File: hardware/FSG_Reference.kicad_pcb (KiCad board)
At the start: 2 copper layers, 63.5 x 38 mm, 73 parts, among them J1 D369-B66-NP4, J3 Screw_Terminal_01x02, K1 SANYOU_SRD_Form_C, Q1 BSS138, Q2 Si2319CDS, Q3 BSS138, U1 LM393, U2 LM393, U3 LM393, U4 LM1117-5.0, U5 LM393, U6 74AHC1G02, U7 MC78M12CDTG DPAK

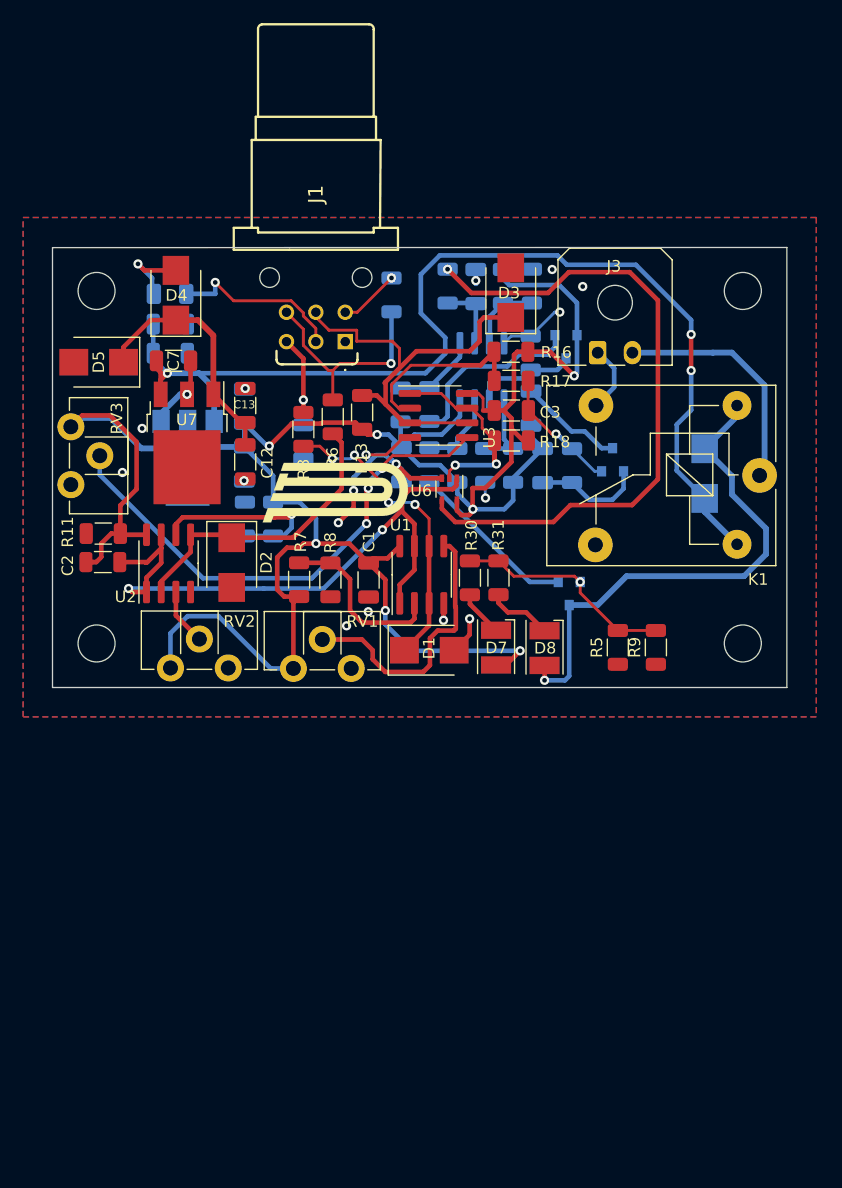
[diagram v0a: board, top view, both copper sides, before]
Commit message: Changed the connector
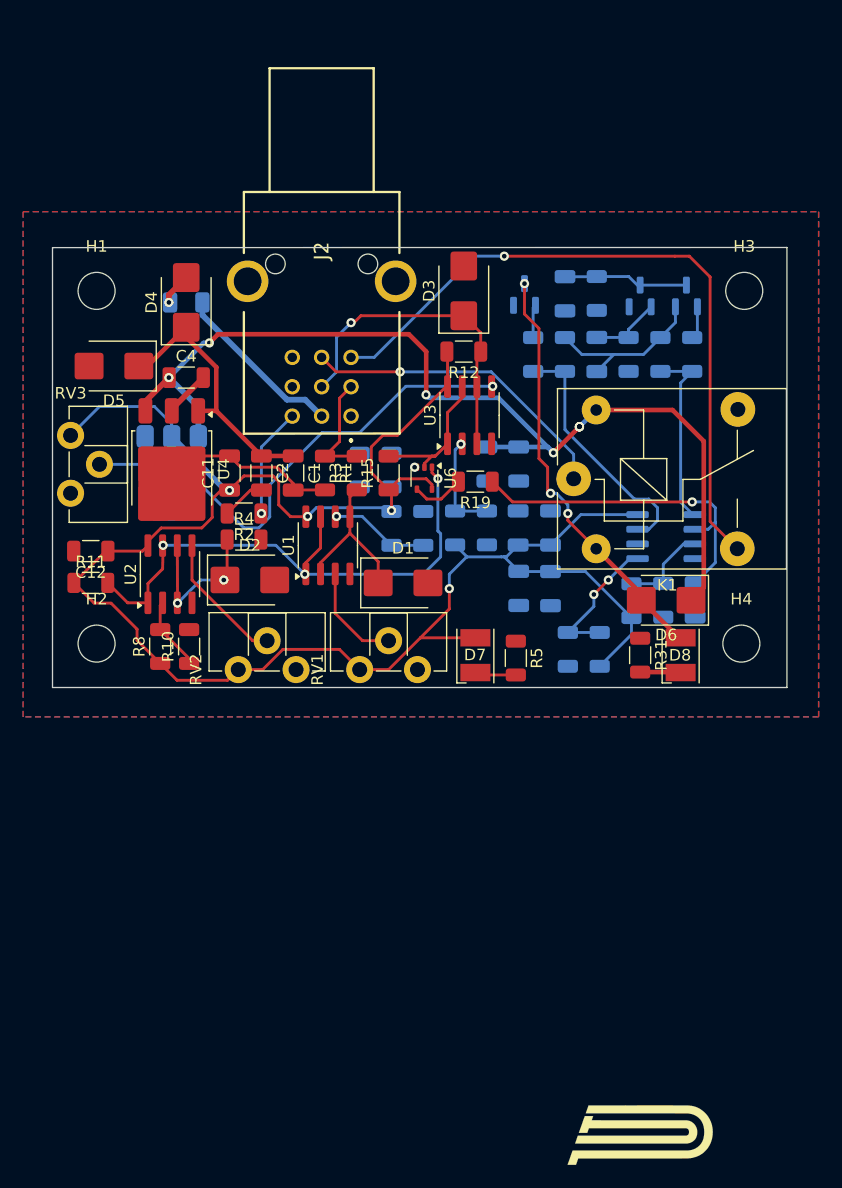
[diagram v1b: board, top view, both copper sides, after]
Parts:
- removed C15: 100n, Capacitor_SMD:C_1206_3216Metric
- removed J1: D369-B66-NP4, Library:D369B66NP4
- removed J3: Screw_Terminal_01x02, Connector_Molex:Molex_Micro-Fit_3.0_43650-0200_1x02_P3.00mm_Horizontal
- removed R17, R18: 10k, Resistor_SMD:R_1206_3216Metric
- removed R30: 1k, Resistor_SMD:R_1206_3216Metric
- added C14: 100n, Capacitor_SMD:C_1206_3216Metric, B.Cu at (140.8, 123.0)
- added J2: D369-G99-NP4, Connector_9pin:D369G99NP4, F.Cu at (123.5, 108.1)
- added R14: 10k, Resistor_SMD:R_1206_3216Metric, B.Cu at (135.2, 117.8)
- added R15: 10k, Resistor_SMD:R_1206_3216Metric, F.Cu at (126.8, 113.0)
- added R2: 100k, Resistor_SMD:R_1206_3216Metric, F.Cu at (114.2, 116.5)
- C1: value 100n -> 10u
- C11, D6, R1, R12, R19: moved to F.Cu
- C12: value 10u -> 100n
- C13: value 100n -> 10u; moved to B.Cu
- C3, C7, R9: moved to B.Cu
- C4: value 10u -> 100n; moved to F.Cu
- R10, R4: value 100k -> 10k; moved to F.Cu
- R13, R6: value 10k -> 100k; moved to B.Cu
- R16: value 100k -> 0R; moved to B.Cu
- R5: value 0R -> 1k
- R7: value 100k -> 10k; moved to B.Cu
- R8: value 10k -> 100k
- U4: value LM1117-5.0 -> MC78M12CDTG DPAK; footprint Package_TO_SOT_SMD:SOT-223 -> Package_TO_SOT_SMD:TO-252-3_TabPin2; moved to F.Cu
- U7: value MC78M12CDTG DPAK -> LM1117-5.0; footprint Package_TO_SOT_SMD:TO-252-3_TabPin2 -> Package_TO_SOT_SMD:SOT-223; moved to B.Cu
- moved G*** 61.5 mm to (148.1, 170.1)
- moved C7 33.1 mm to (137.9, 117.8), turned to 90 degrees
- moved C5 33.1 mm to (153.2, 124.0), turned to -90 degrees
- moved R22 29.4 mm to (150.5, 124.0), turned to -90 degrees
- moved R21 29.4 mm to (147.8, 124.0), turned to 90 degrees
- moved C13 28.4 mm to (138.0, 123.0), turned to -90 degrees
- moved R9 27.5 mm to (127.0, 112.8)
- moved Q3 26.1 mm to (138.5, 97.6), turned to 90 degrees
- moved R4 24.7 mm to (114.2, 118.8), turned to 0 degrees
- moved C9 24.2 mm to (138.0, 112.2), turned to -90 degrees
- moved R12 23.8 mm to (133.2, 102.5), turned to 180 degrees
- moved R28 23.1 mm to (153.0, 102.8), turned to -90 degrees
- moved R26 22.9 mm to (150.2, 102.8), turned to -90 degrees
- moved U5 21.4 mm to (150.8, 118.5), turned to 180 degrees
- moved C8 21.0 mm to (135.2, 112.2)
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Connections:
- net /Comparators/Brake1 renamed Brake2
- net /Comparators/Brake1Logic renamed BrakeLogic
- net /Comparators/Error renamed Error
- net /Comparators/TPSLogic renamed CSLogic
- net Net-(Q3-G) renamed Relay Drive Signal
- C1 pad 1: +5V -> Net-(D4-K)
- C12 pad 1: Net-(D4-K) -> +5V
- C13 pad 1: Net-(D4-K) -> +5V
- C2 pad 1: +5V -> Net-(D4-K)
- C7 pad 1: +12V -> +5V
- C8 pad 1: +5V -> +12V
- C9 pad 1: +5V -> +12V
- D3 pad 1: /Comparators/TPS -> ControlSignal
- F1 pad 2: LV_in -> +24V
- K1 pad 1: Net-(J3-Pin_2) -> Relay2
- K1 pad 3: Net-(J3-Pin_1) -> Relay1
- R10 pad 1: +5V -> Net-(U2A--)
- R10 pad 2: Net-(U2B--) -> GND
- R12 pad 1: Net-(U2B--) -> ControlSignal
- R12 pad 2: GND -> +5V
- R13 pad 1: /Comparators/TPS -> +5V
- R13 pad 2: +5V -> Net-(U3A--)
- R16 pad 1: +5V -> GND
- R16 pad 2: Net-(U3A--) -> GND
- R4 pad 1: /Comparators/Brake2 -> Net-(D2-A1)
- R4 pad 2: GND -> Brake1
- R5 pad 2: GND -> Net-(D7-K)
- R6 pad 1: Net-(D2-A1) -> +5V
- R6 pad 2: /Comparators/Brake2 -> Net-(U1B--)
- R7 pad 1: +5V -> Net-(U1B--)
- R7 pad 2: Net-(U1A--) -> GND
- R8 pad 1: Net-(U1A--) -> +5V
- R8 pad 2: GND -> Net-(U2A--)
- RV1 pad 2: Net-(U1B-+) -> Net-(U1A-+)
- RV2 pad 2: Net-(U2A-+) -> Net-(U2B-+)
- U1 pad 2: Net-(U1A--) -> Net-(D1-A1)
- U1 pad 3: Net-(D1-A1) -> Net-(U1A-+)
- U1 pad 5: Net-(U1B-+) -> Net-(D1-A1)
- U1 pad 6: Net-(D1-A1) -> Net-(U1B--)
- U2 pad 2: Net-(D2-A1) -> Net-(U2A--)
- U2 pad 3: Net-(U2A-+) -> Net-(D2-A1)
- U2 pad 5: Net-(D2-A1) -> Net-(U2B-+)
- U2 pad 6: Net-(U2B--) -> Net-(D2-A1)
- U3 pad 3: /Comparators/TPS -> ControlSignal
- U3 pad 6: /Comparators/TPS -> ControlSignal
- U4 pad 1: GND -> Net-(D4-K)
- U4 pad 2: +5V -> GND
- U7 pad 1: Net-(D4-K) -> GND
- U7 pad 2: GND -> +5V
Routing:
- net Relay1: track 0.00 -> 59.9 mm, vias 0 -> 1
- net GND: track 76.0 -> 21.4 mm, vias 21 -> 1
- net Error: track 57.7 -> 4.56 mm, vias 1 -> 0
- net /Comparators/TPS: track 38.7 -> 0.00 mm
- net +5V: track 211.0 -> 178.6 mm, vias 7 -> 4
- net ControlSignal: track 0.00 -> 28.4 mm, vias 0 -> 1
- net Relay2: track 0.00 -> 27.4 mm, vias 0 -> 1
- net Net-(U1B-+): track 23.9 -> 0.00 mm
- net Net-(U5A--): track 5.93 -> 29.5 mm, vias 0 -> 1
- net Net-(J3-Pin_2): track 20.6 -> 0.00 mm
- net /Comparators/Brake2: track 19.2 -> 0.00 mm, vias 1 -> 0
- net Net-(U2B--): track 17.7 -> 0.00 mm, vias 1 -> 0
- net Net-(U1A--): track 15.2 -> 0.00 mm
- net LV_in: track 15.1 -> 0.00 mm, vias 1 -> 0
- net +24V: track 0.00 -> 15.0 mm
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- added copper zone on In1.Cu, net GND
- added copper zone on In2.Cu, net GND
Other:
- copper layers 2 -> 4

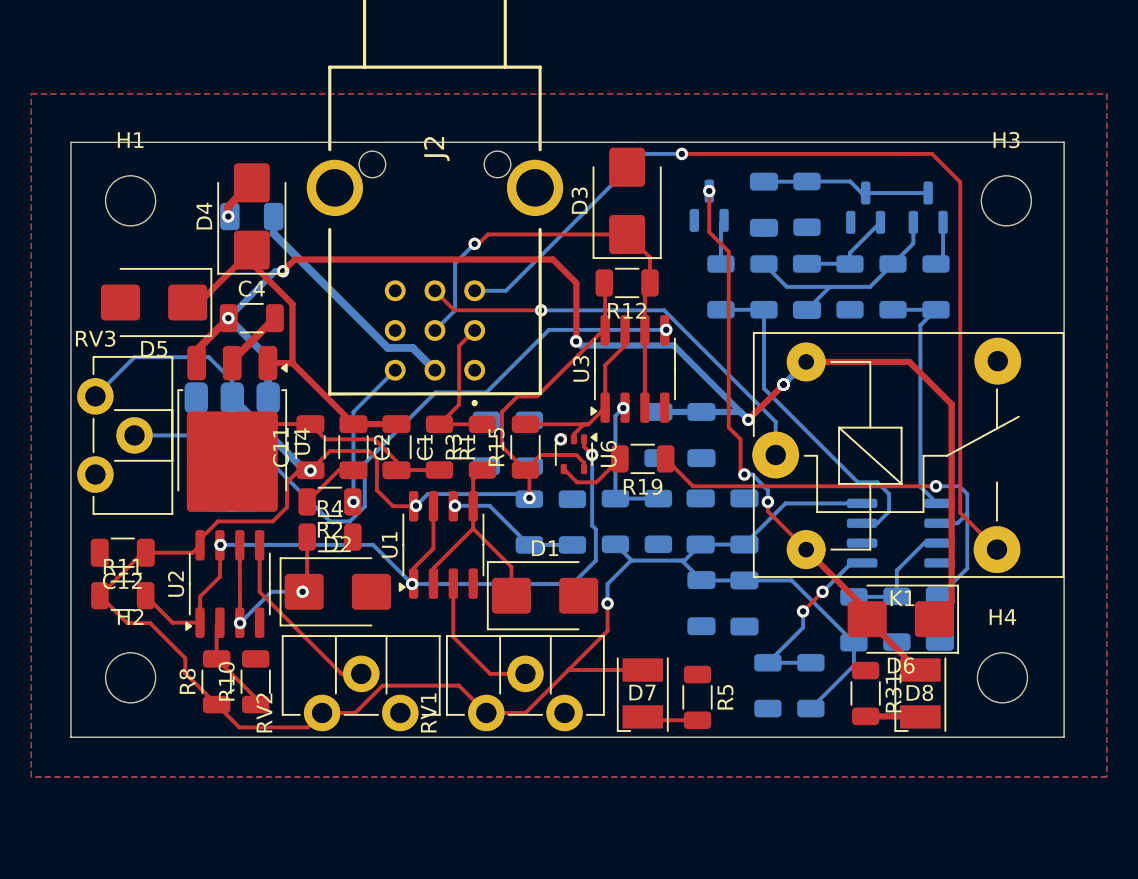
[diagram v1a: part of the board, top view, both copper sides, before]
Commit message: fixed the error of the connector, now 0 errors
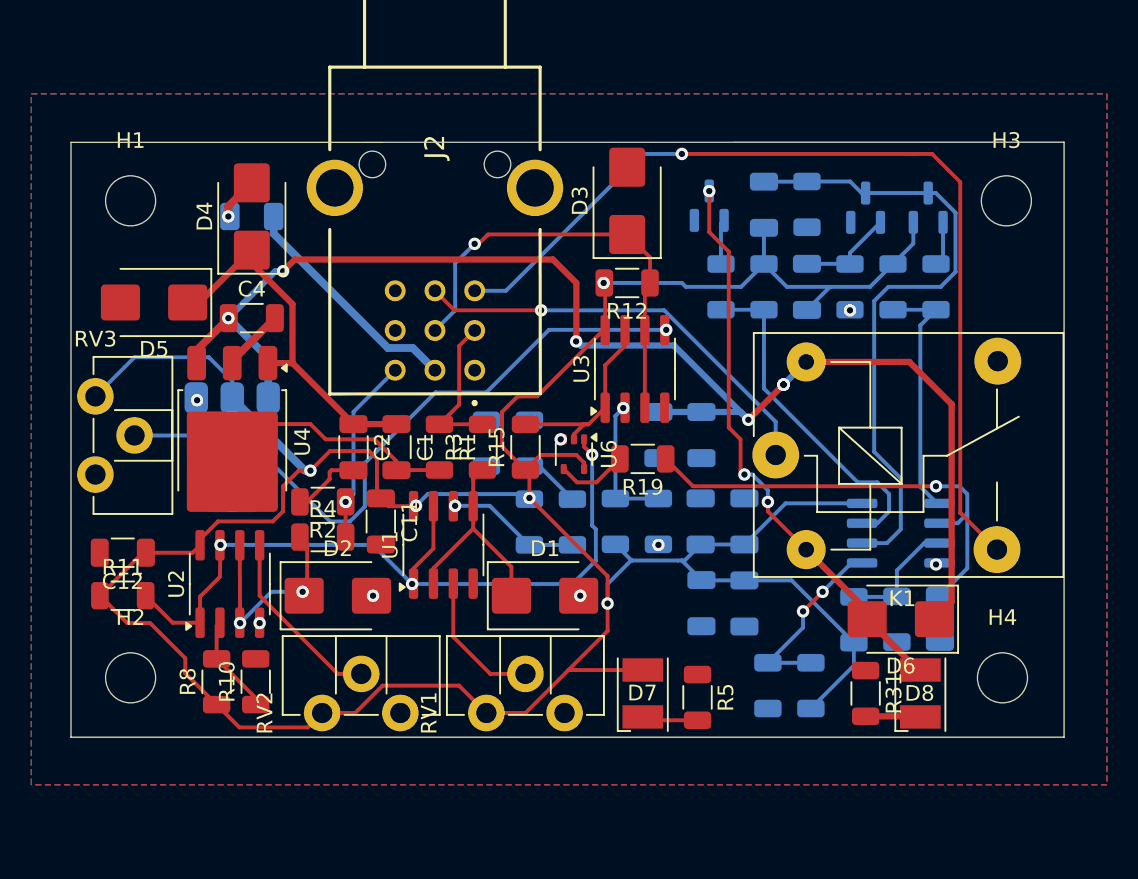
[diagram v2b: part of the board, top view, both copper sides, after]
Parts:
- moved C11 6.54 mm to (117.5, 117.8), turned to -90 degrees
- moved R2 0.46 mm to (113.8, 116.5)
- moved R4 0.46 mm to (113.8, 118.8)
- moved D2 0.25 mm to (114.8, 122.5)
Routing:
- net Net-(Q1-D): track 10.8 -> 41.0 mm
- net +5V: track 178.6 -> 200.9 mm, vias 4 -> 5
- net GND: track 21.4 -> 25.7 mm, vias 1 -> 8
- net Brake1: track 9.65 -> 12.4 mm
